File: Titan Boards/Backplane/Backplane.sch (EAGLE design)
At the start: 20 parts

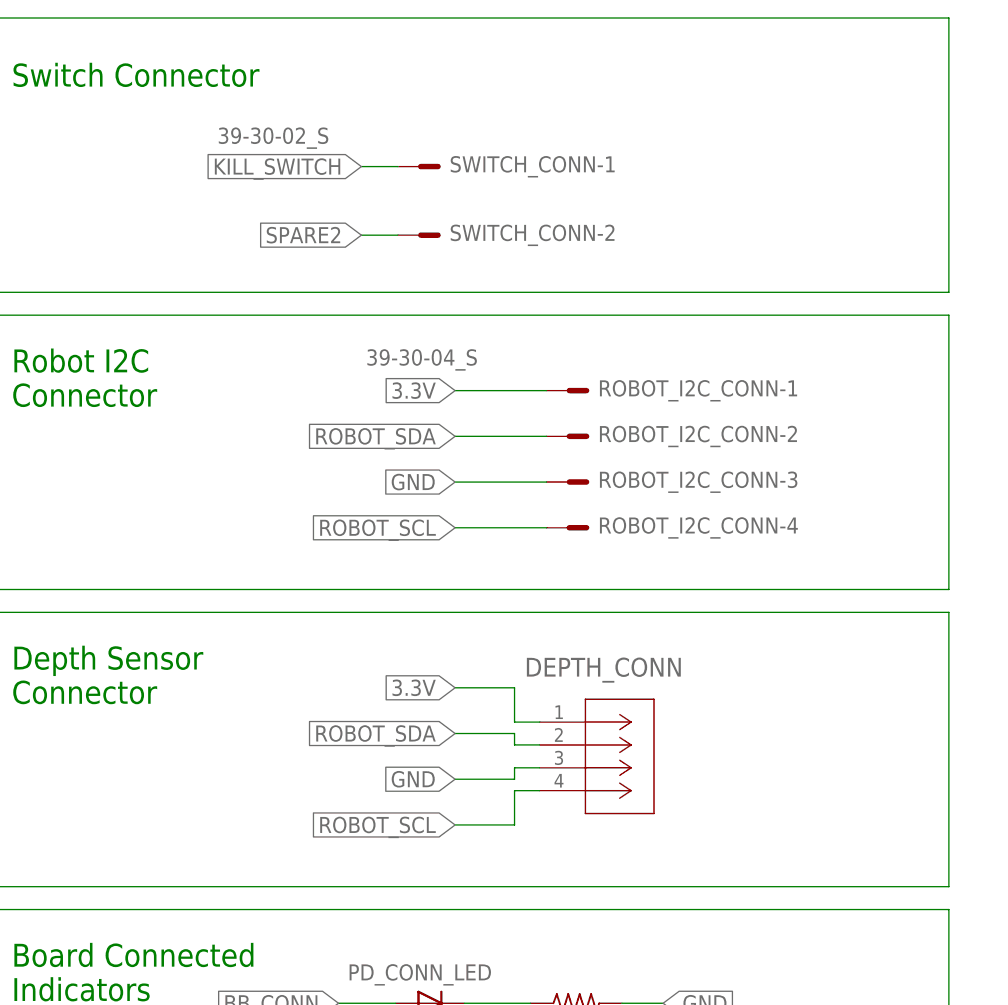
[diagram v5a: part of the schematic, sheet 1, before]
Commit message: Backplane design review changes
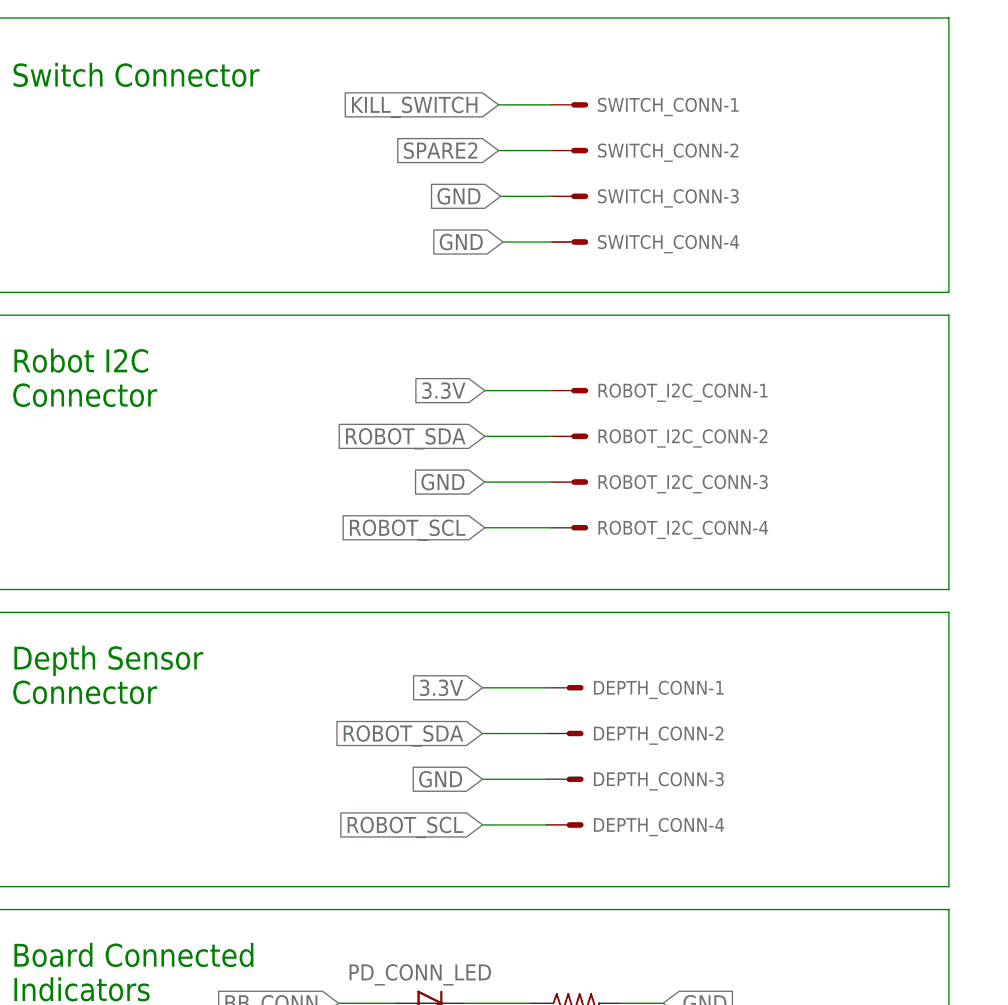
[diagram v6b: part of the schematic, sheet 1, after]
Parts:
- DEPTH_CONN: value DF13-4P-1.25DSA -> (none); device DF13-4P-125DSA_Connector:DF13-4P-1.25DSA -> con-molex-2:555X-4V
- ROBOT_I2C_CONN: value 39-30-04_S -> (none); device con-molex-mini-fit:39-30-04_S -> con-molex-2:555X-4V
- SWITCH_CONN: value 39-30-02_S -> (none); device con-molex-mini-fit:39-30-02_S -> con-molex-2:555X-4V
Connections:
- net 3.3V: now also DEPTH_CONN-1.S, ROBOT_I2C_CONN-1.S; no longer DEPTH_CONN.1, ROBOT_I2C_CONN-1.P
- net GND: now also DEPTH_CONN-3.S, ROBOT_I2C_CONN-3.S, SWITCH_CONN-3.S, SWITCH_CONN-4.S; no longer DEPTH_CONN.3, ROBOT_I2C_CONN-3.P
- net KILL_SWITCH: now also SWITCH_CONN-1.S; no longer SWITCH_CONN-1.P
- net ROBOT_SCL: now also DEPTH_CONN-4.S, ROBOT_I2C_CONN-4.S; no longer DEPTH_CONN.4, ROBOT_I2C_CONN-4.P
- net ROBOT_SDA: now also DEPTH_CONN-2.S, ROBOT_I2C_CONN-2.S; no longer DEPTH_CONN.2, ROBOT_I2C_CONN-2.P
- net SPARE2: now also SWITCH_CONN-2.S; no longer SWITCH_CONN-2.P
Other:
- moved on the sheet: SWITCH_CONN-1, SWITCH_CONN-2

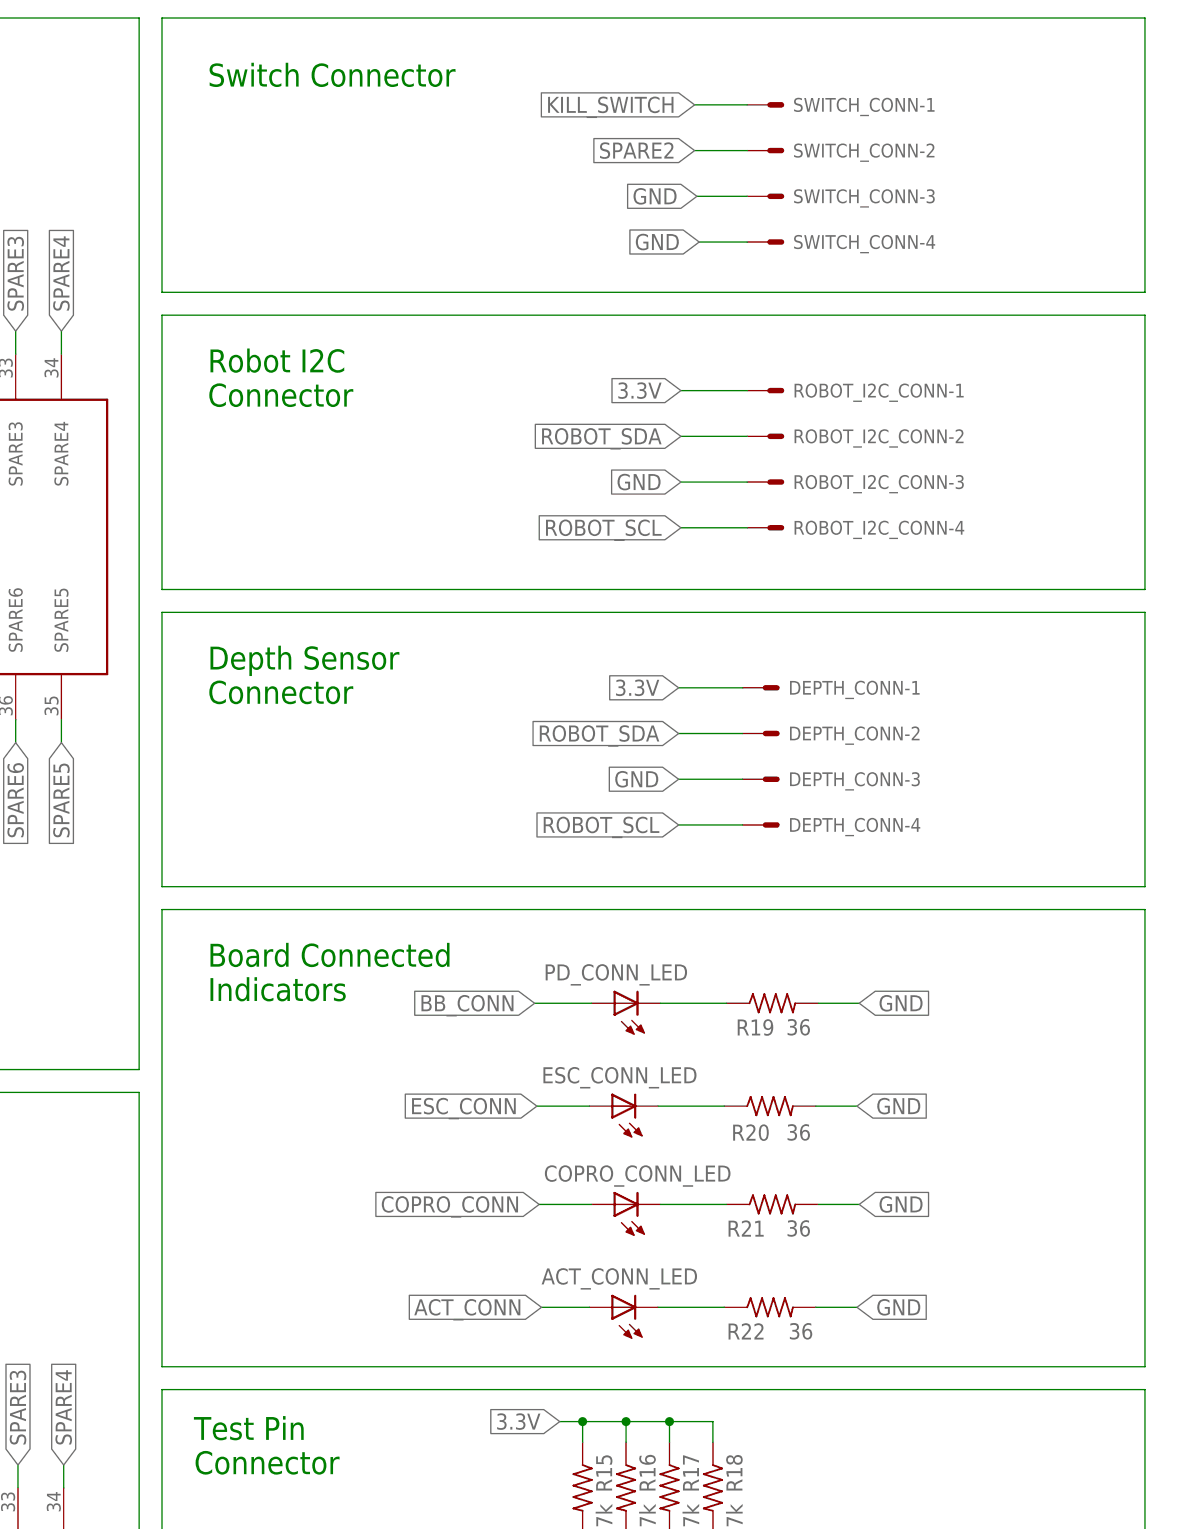
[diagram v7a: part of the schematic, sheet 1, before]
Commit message: Acoustics connector on titan backplane
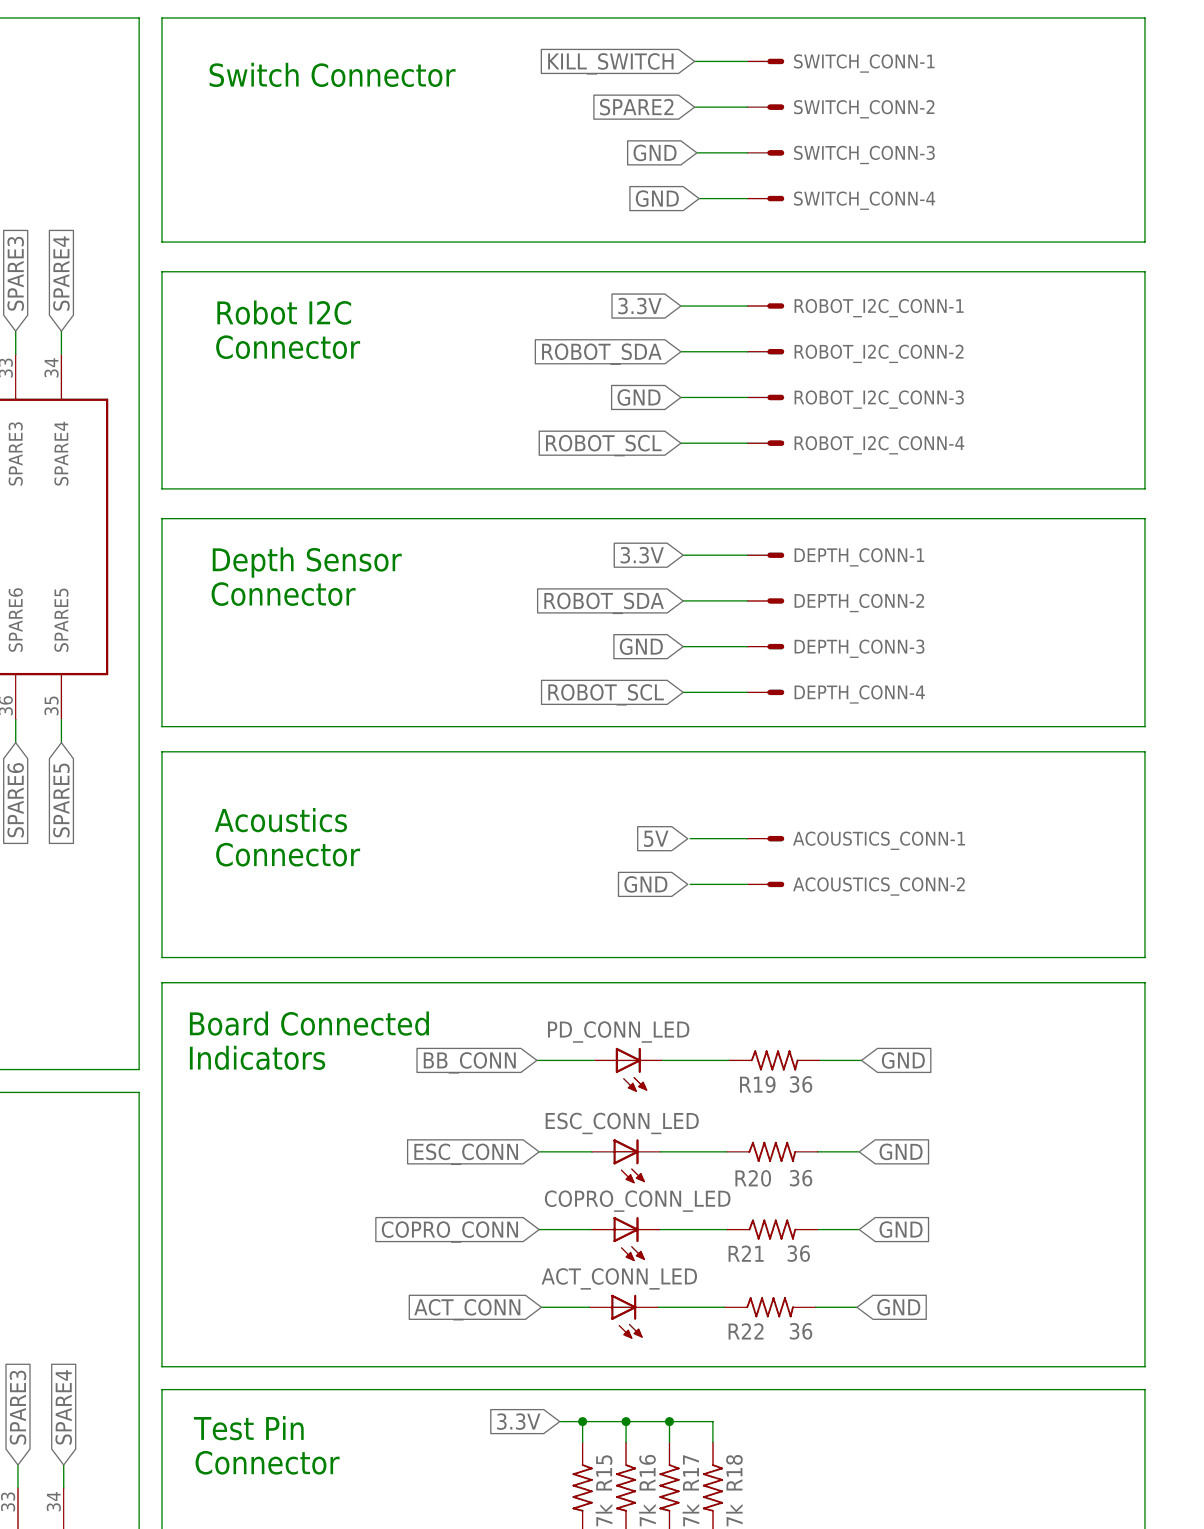
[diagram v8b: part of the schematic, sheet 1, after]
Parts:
- added ACOUSTICS_CONN: (no value), con-molex-2:555X-2V
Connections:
- net 5V: now also ACOUSTICS_CONN-1.S
- net GND: now also ACOUSTICS_CONN-2.S
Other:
- note added: "Acoustics Connector"
- moved on the sheet: COPRO_CONN_LED, DEPTH_CONN-1, DEPTH_CONN-2, DEPTH_CONN-3, DEPTH_CONN-4, ESC_CONN_LED, PD_CONN_LED, R19, R20, R21, ROBOT_I2C_CONN-1, ROBOT_I2C_CONN-2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
